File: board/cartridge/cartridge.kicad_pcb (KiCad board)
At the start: 4 copper layers, 66 x 52.8 mm, 24 parts, among them J1 Foxconn_WQ21823-DES1-7F, U1 AMS1117-3.3, U2 STM32G0B0RETx, U3 74LVC1G07, U4 NAU8814Y

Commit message: Place and route MCU power and crystal.
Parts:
- added Y1: X322516MLB4SI, Crystal:Crystal_SMD_3225-4Pin_3.2x2.5mm, F.Cu at (130.0, 102.4)
- C3, C4: value 20p -> 18p
- P1: value ~ -> CardEdge
- moved C6 35.6 mm to (126.2, 100.6)
- moved C5 33.7 mm to (126.2, 102.1)
- moved C3 27.5 mm to (130.1, 104.9)
- moved C4 26.4 mm to (133.0, 102.3), turned to -90 degrees
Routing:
- net /D3: track 31.7 -> 0.00 mm, vias 2 -> 0
- net /D2: track 29.7 -> 0.00 mm, vias 1 -> 0
- net /D1: track 29.1 -> 0.00 mm, vias 2 -> 0
- net /D0: track 28.2 -> 0.00 mm, vias 1 -> 0
- net /D4: track 28.2 -> 0.00 mm, vias 1 -> 0
- net /D6: track 27.1 -> 0.00 mm, vias 1 -> 0
- net /D5: track 29.5 -> 7.11 mm, vias 2 -> 1
- net /D7: track 28.4 -> 9.20 mm, vias 2 -> 1
- net GND: track 30.2 -> 43.3 mm, vias 6 -> 8
- net +3V3: track 8.95 -> 18.4 mm, vias 0 -> 1
- net /OSC_OUT: track 0.00 -> 8.21 mm
- net /OSC_IN: track 0.00 -> 8.11 mm
- net /SWD_~{RST}: track 0.00 -> 4.93 mm

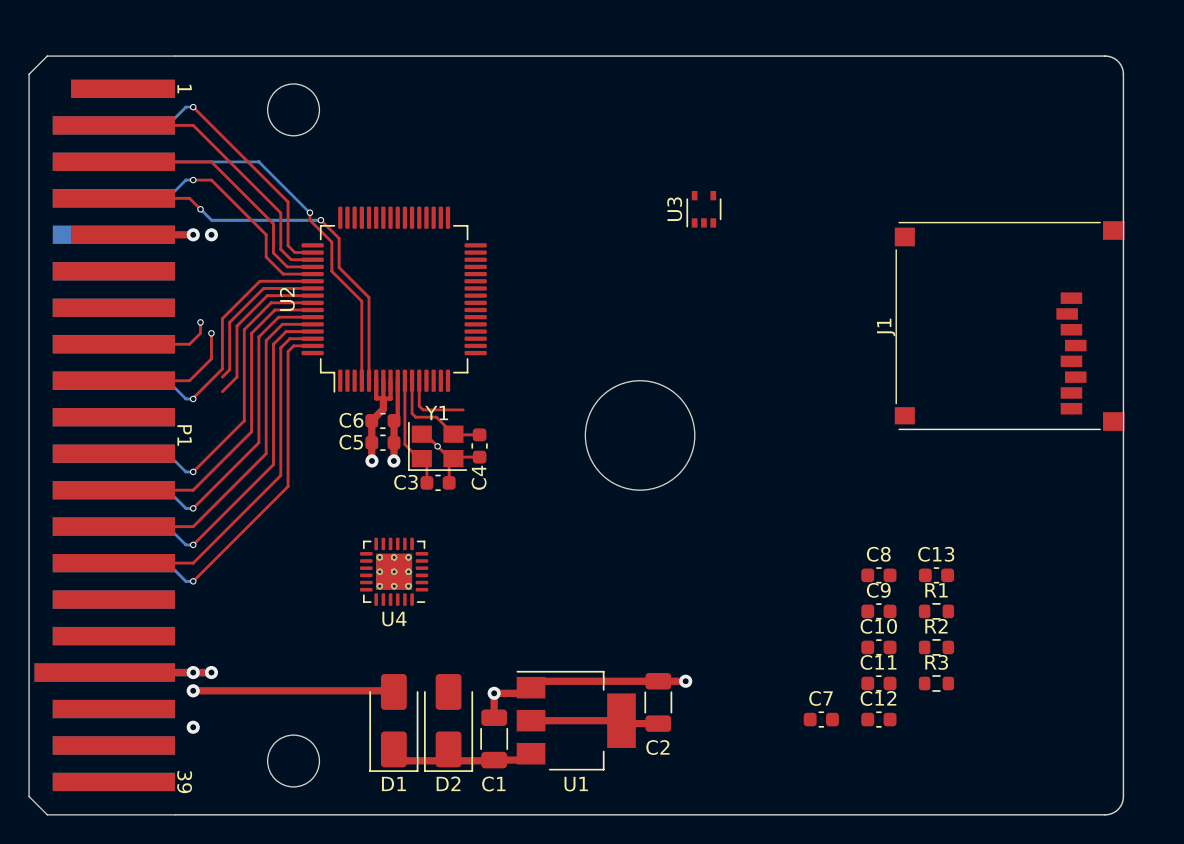
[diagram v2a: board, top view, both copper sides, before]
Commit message: Choose parts for everything plus more routing.
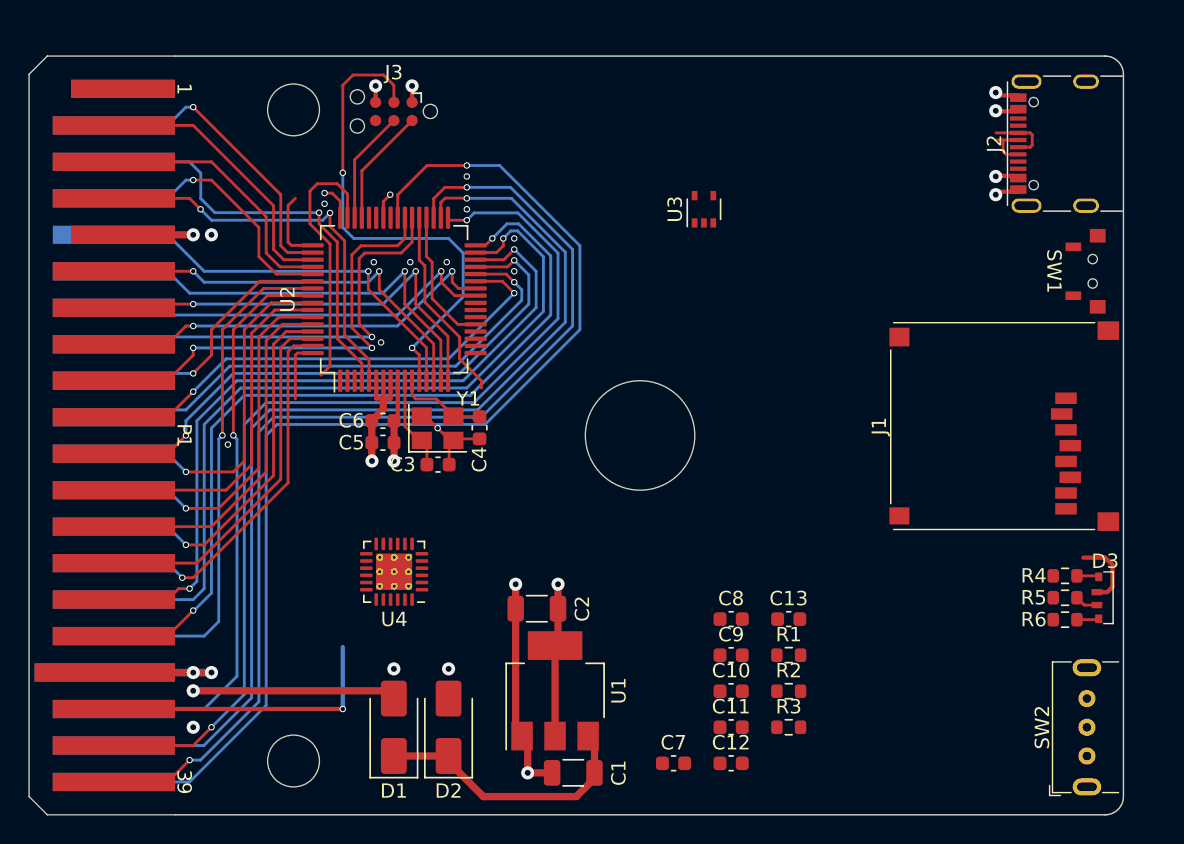
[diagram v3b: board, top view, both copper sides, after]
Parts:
- added D3: FM-3510RGBA-SG, 0Project:FM-3510RGBA-SG, F.Cu at (176.5, 112.9)
- added J2: KH-TYPE-C-16P, 0Project:KH-TYPE-C-16P, F.Cu at (174.1, 81.3)
- added J3: TC2030-NL, Connector:Tag-Connect_TC2030-IDC-NL_2x03_P1.27mm_Vertical, F.Cu at (127.0, 79.0)
- added R4: 100R, Resistor_SMD:R_0603_1608Metric, F.Cu at (173.7, 111.4)
- added R5: 100R, Resistor_SMD:R_0603_1608Metric, F.Cu at (173.7, 112.9)
- added R6: 100R, Resistor_SMD:R_0603_1608Metric, F.Cu at (173.7, 114.4)
- added SW1: TSA002A3518B, 0Project:TSA002A3518B, F.Cu at (175.3, 90.2)
- added SW2: SK12D07VG4, 0Project:SK12D07VG4, F.Cu at (175.3, 121.9)
- D1, D2: value SS12-AT -> SS14
- moved C7 10.7 mm to (146.5, 124.4)
- moved C10 10.7 mm to (150.5, 119.4)
- moved C11 10.7 mm to (150.5, 121.9)
- moved C12 10.7 mm to (150.5, 124.4)
- moved C13 10.7 mm to (154.5, 114.4)
- moved C8 10.7 mm to (150.5, 114.4)
- moved C9 10.7 mm to (150.5, 116.9)
- moved R1 10.7 mm to (154.5, 116.9)
- moved R2 10.7 mm to (154.5, 119.4)
- moved R3 10.7 mm to (154.5, 121.9)
- moved C2 10.7 mm to (137.0, 113.7), turned to 180 degrees
- moved J1 6.98 mm to (161.8, 108.0)
- moved C1 6.00 mm to (139.5, 125.1), turned to 180 degrees
- moved U1 2.55 mm to (138.2, 119.4), turned to 90 degrees
- moved C4 1.27 mm to (133.0, 101.1)
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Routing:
- net /~{SLEN}: track 0.00 -> 79.8 mm, vias 0 -> 1
- net /A15: track 0.00 -> 74.6 mm, vias 0 -> 2
- net /A14: track 0.00 -> 70.9 mm, vias 0 -> 1
- net /A13: track 0.00 -> 68.0 mm, vias 0 -> 2
- net /A12: track 0.00 -> 57.3 mm, vias 0 -> 2
- net /A11: track 0.00 -> 55.1 mm, vias 0 -> 1
- net /A10: track 0.00 -> 52.0 mm, vias 0 -> 2
- net /A2: track 0.00 -> 40.1 mm, vias 0 -> 2
- net /A1: track 0.00 -> 36.2 mm, vias 0 -> 1
- net /A0: track 0.00 -> 34.5 mm, vias 0 -> 2
- net /D6: track 0.00 -> 30.9 mm, vias 0 -> 1
- net /D3: track 0.00 -> 30.6 mm, vias 0 -> 2
- net /D2: track 0.00 -> 30.2 mm, vias 0 -> 1
- net /SWD_~{RST}: track 4.93 -> 34.9 mm, vias 0 -> 2
- net /~{SCS}: track 11.1 -> 40.3 mm, vias 0 -> 1
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
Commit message: Update footprint positions to match JLCPCB.
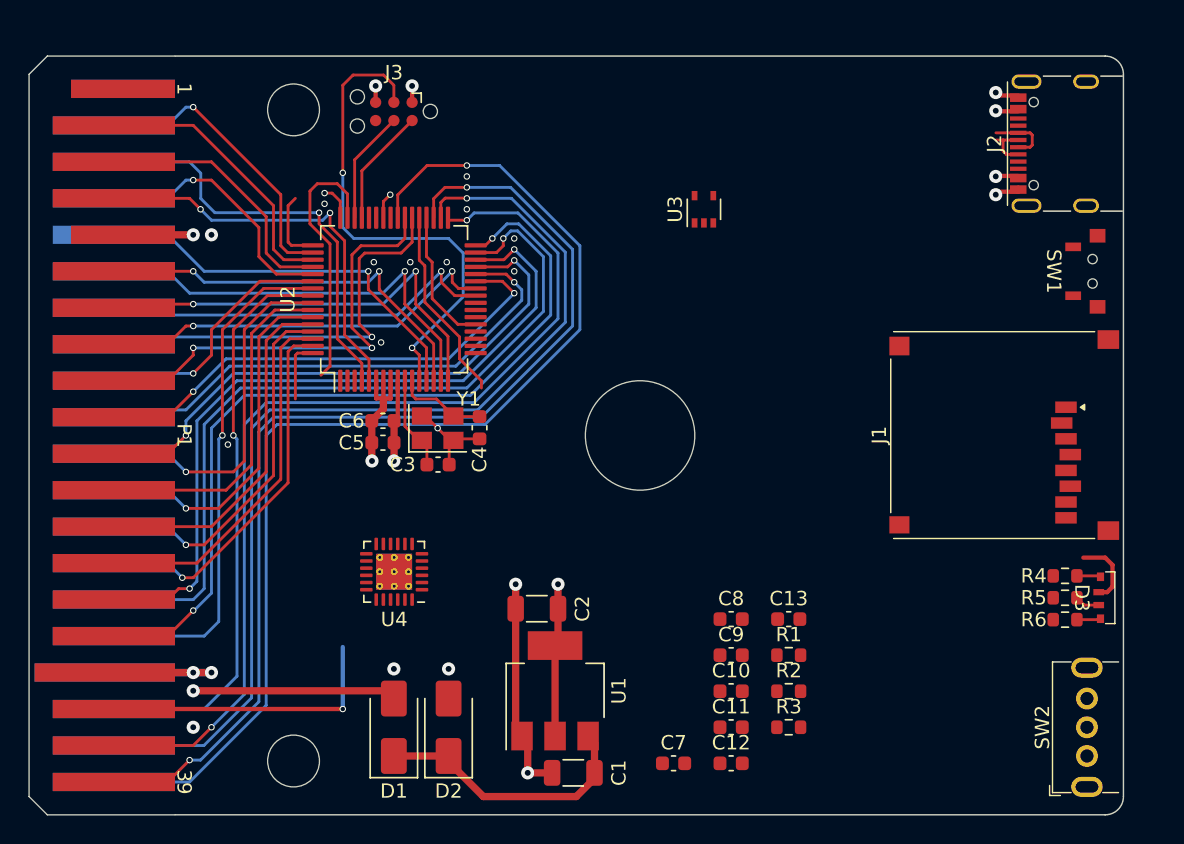
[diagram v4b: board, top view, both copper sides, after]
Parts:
- moved J1 10.0 mm to (169.6, 101.6)
- moved J2 1.31 mm to (172.8, 81.3)
- moved D3 0.39 mm to (176.1, 112.9)
- moved SW1 0.11 mm to (175.2, 90.2)

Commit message: Rip up and try routing as 2 layer.
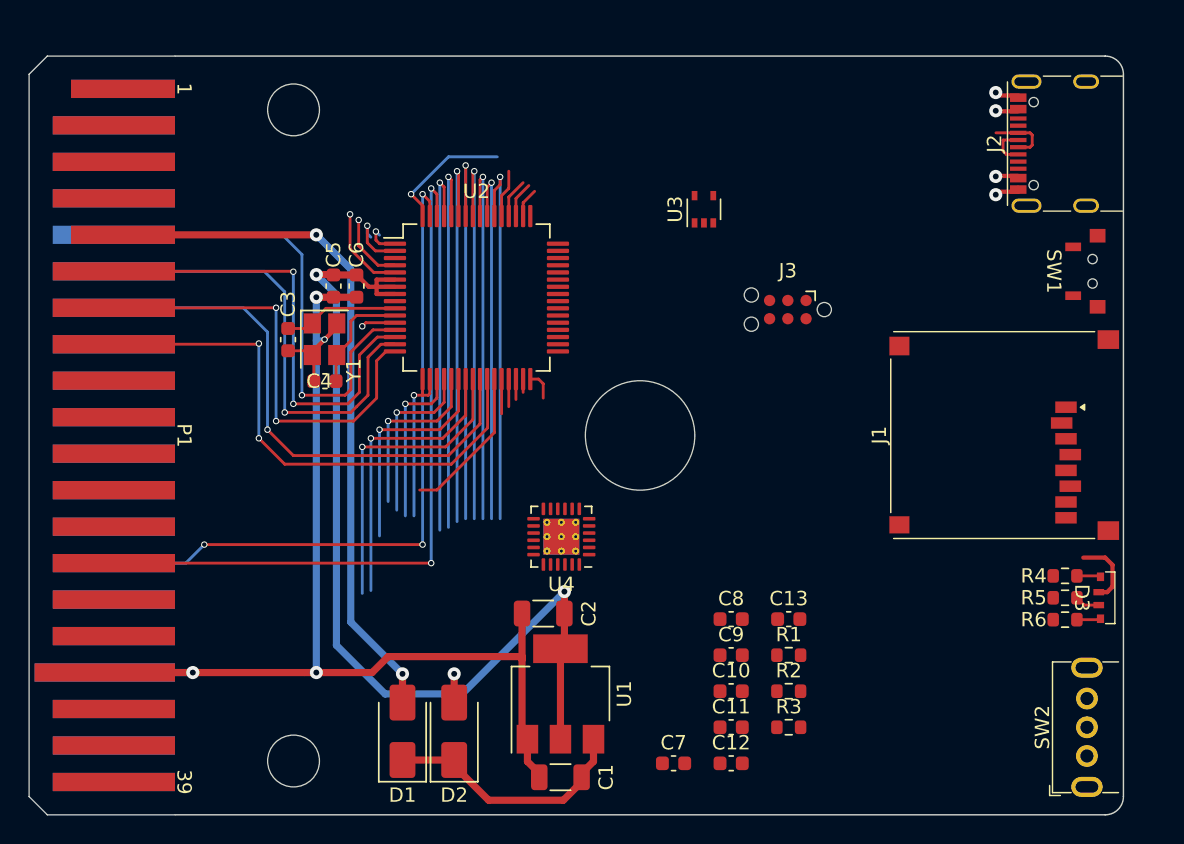
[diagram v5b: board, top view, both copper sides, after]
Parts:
- moved J3 30.7 mm to (154.4, 92.8)
- moved C3 13.6 mm to (119.6, 94.9), turned to -90 degrees
- moved U4 11.9 mm to (138.7, 108.7)
- moved C5 11.4 mm to (122.8, 91.2), turned to -90 degrees
- moved C4 11.2 mm to (122.2, 97.8), turned to 180 degrees
- moved Y1 10.0 mm to (122.2, 94.9), turned to -90 degrees
- moved C6 9.56 mm to (124.4, 91.2), turned to -90 degrees
- moved U2 5.73 mm to (132.8, 92.0), turned to 0 degrees
- moved C1 0.95 mm to (138.6, 125.4)
- moved D1 0.66 mm to (127.6, 122.2)
- moved C2 0.56 mm to (137.4, 114.0)
- moved D2 0.48 mm to (131.2, 122.2)
- moved U1 0.43 mm to (138.6, 119.6)
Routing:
- net /~{SLEN}: track 79.8 -> 0.00 mm, vias 1 -> 0
- net /A15: track 74.6 -> 0.00 mm, vias 2 -> 0
- net /A14: track 70.9 -> 0.00 mm, vias 1 -> 0
- net /A13: track 68.0 -> 0.00 mm, vias 2 -> 0
- net /A12: track 57.3 -> 2.03 mm, vias 2 -> 0
- net /A11: track 55.1 -> 0.92 mm, vias 1 -> 0
- net /A10: track 52.0 -> 1.42 mm, vias 2 -> 0
- net +3V3: track 26.3 -> 71.4 mm, vias 3 -> 2
- net GND: track 47.9 -> 87.5 mm, vias 23 -> 6
- net /A2: track 40.1 -> 1.92 mm, vias 2 -> 0
- net /A1: track 36.2 -> 2.42 mm, vias 1 -> 0
- net /SWD_~{RST}: track 34.9 -> 2.38 mm, vias 2 -> 1
- net /D7: track 31.9 -> 0.00 mm, vias 2 -> 0
- net /D6: track 30.9 -> 0.00 mm, vias 1 -> 0
- net /E: track 29.7 -> 4.88 mm
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- removed copper zone on In1.Cu, net GND
- removed copper zone on In2.Cu, net GND
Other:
- copper layers 4 -> 2

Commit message: Adjust layout based on an actual Tandy cartridge.
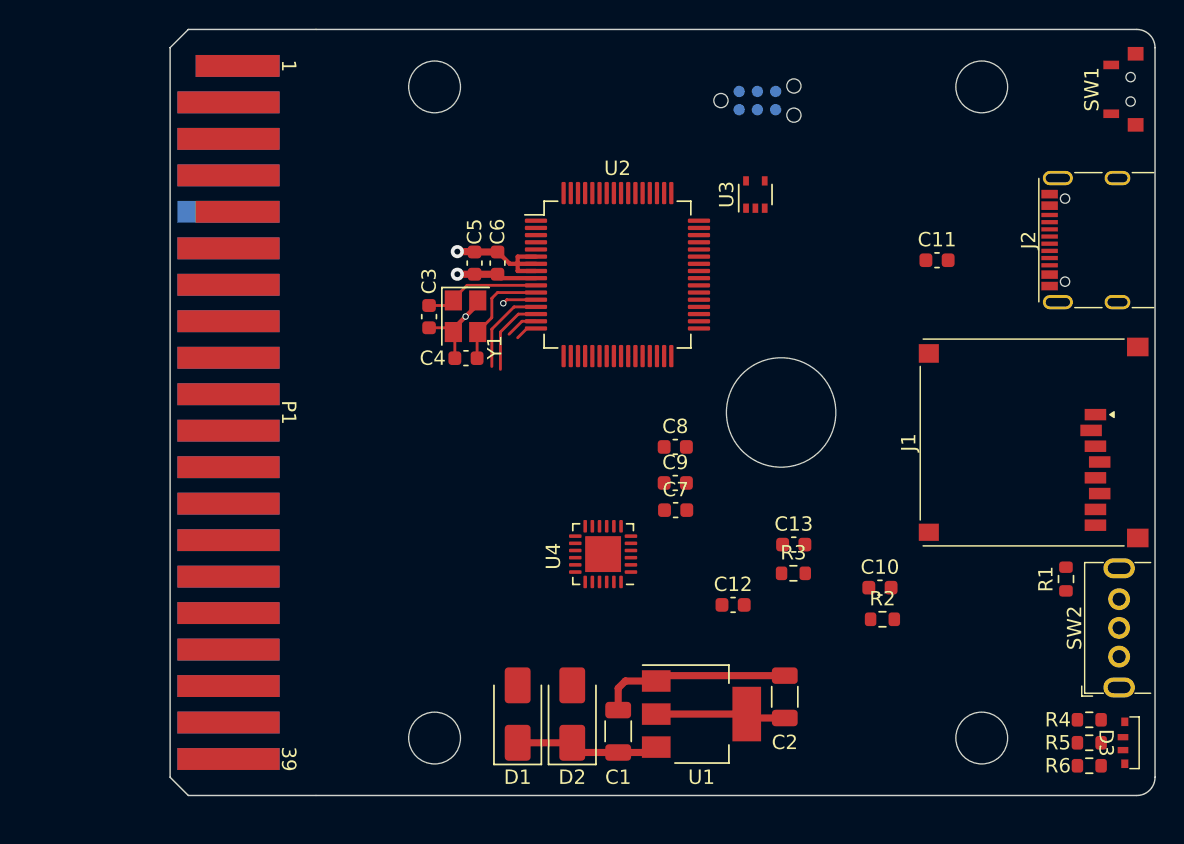
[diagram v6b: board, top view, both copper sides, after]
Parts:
- added MH1: CoCo_MountingHole, 0Local:CoCo_MountingHole, F.Cu at (129.8, 77.3)
- added MH1: CoCo_MountingHole, 0Local:CoCo_MountingHole, F.Cu at (167.9, 77.3)
- added MH1: CoCo_MountingHole, 0Local:CoCo_MountingHole, F.Cu at (167.9, 122.7)
- added MH2: CoCo_MountingHole, 0Local:CoCo_MountingHole, F.Cu at (129.8, 122.7)
- added MH5: CoCo_ClearanceHole, 0Local:CoCo_ClearanceHole, F.Cu at (154.0, 100.0)
- J1: value Foxconn_WQ21823-DES1-7F -> WQ21823-DES1-7F
- J3: moved to B.Cu
- U4: footprint Package_DFN_QFN:VQFN-24-1EP_4x4mm_P0.5mm_EP2.5x2.5mm_ThermalVias -> Package_DFN_QFN:VQFN-24-1EP_4x4mm_P0.5mm_EP2.5x2.5mm
- moved C11 35.5 mm to (164.8, 89.4)
- moved R1 20.0 mm to (173.8, 111.6), turned to 90 degrees
- moved C2 17.8 mm to (154.2, 119.8), turned to 90 degrees
- moved C7 17.6 mm to (146.6, 106.8)
- moved J3 14.7 mm to (152.3, 78.3), turned to 0 degrees
- moved SW1 12.9 mm to (177.8, 77.5)
- moved C10 12.6 mm to (160.8, 112.2)
- moved C9 12.6 mm to (146.6, 104.9)
- moved C8 12.6 mm to (146.6, 102.4)
- moved C12 11.0 mm to (150.6, 113.4)
- moved R3 10.7 mm to (154.8, 111.2)
- moved R6 10.3 mm to (175.4, 124.6)
- moved D3 10.2 mm to (177.8, 123.0)
- moved R5 10.2 mm to (175.4, 123.0)
- moved R4 10.2 mm to (175.4, 121.4)
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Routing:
- net GND: track 87.5 -> 25.7 mm, vias 6 -> 2
- net +3V3: track 71.4 -> 18.4 mm, vias 2 -> 1
- net /A8: track 50.3 -> 0.00 mm, vias 2 -> 0
- net +5V: track 48.5 -> 0.00 mm, vias 2 -> 0
- net /A9: track 48.2 -> 0.00 mm, vias 3 -> 0
- net /D5: track 37.8 -> 0.04 mm, vias 2 -> 0
- net /D4: track 37.8 -> 0.00 mm, vias 1 -> 0
- net /D2: track 32.1 -> 2.25 mm, vias 1 -> 0
- net /D3: track 31.0 -> 1.54 mm, vias 2 -> 0
- net /A4: track 28.1 -> 0.00 mm, vias 1 -> 0
- net /A5: track 27.6 -> 0.00 mm, vias 1 -> 0
- net /A3: track 27.4 -> 0.00 mm, vias 1 -> 0
- net /A6: track 27.2 -> 0.00 mm, vias 1 -> 0
- net /D0: track 33.3 -> 6.32 mm, vias 1 -> 0
- net /R/~{W}: track 26.7 -> 0.00 mm, vias 1 -> 0
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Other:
- board size 66 x 52.8 mm -> 58.4 x 53.3 mm

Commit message: Another attempt at routing.
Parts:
- J3: moved to F.Cu
- moved C10 29.3 mm to (133.0, 103.0), turned to -90 degrees
- moved R2 28.8 mm to (134.6, 103.0), turned to -90 degrees
- moved C13 17.7 mm to (137.2, 107.9)
- moved R3 14.8 mm to (140.4, 107.9), turned to 180 degrees
- moved C11 12.6 mm to (176.6, 93.8)
- moved C12 12.5 mm to (140.4, 106.3)
- moved C9 9.49 mm to (137.2, 106.3), turned to 180 degrees
- moved U4 8.40 mm to (139.1, 101.8)
- moved J3 7.22 mm to (154.4, 85.2), turned to 180 degrees
- moved U3 5.53 mm to (149.8, 79.8), turned to -90 degrees
- moved C7 4.64 mm to (144.1, 102.9)
- moved C8 3.67 mm to (143.4, 100.6), turned to 90 degrees
- moved C3 0.40 mm to (129.5, 92.9)
- moved C4 0.40 mm to (132.0, 95.8)
- moved U2 0.40 mm to (142.6, 90.0)
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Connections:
- net /USB_DM renamed /USB_DN
- U4 pad 20: unconnected-(U4-VDDSPK-Pad20) -> +3V3
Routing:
- net GND: track 25.7 -> 176.5 mm, vias 2 -> 8
- net VBUS: track 0.00 -> 76.6 mm, vias 0 -> 3
- net +5V: track 0.00 -> 69.7 mm, vias 0 -> 2
- net +3V3: track 18.4 -> 67.6 mm, vias 1 -> 3
- net /~{NMI}: track 0.00 -> 37.4 mm, vias 0 -> 1
- net /~{HALT}: track 0.00 -> 36.4 mm
- net /~{RESET}: track 0.00 -> 35.1 mm, vias 0 -> 1
- net /~{CART}: track 0.00 -> 33.3 mm, vias 0 -> 1
- net /USB_DN: track 0.00 -> 27.1 mm
- net /E: track 0.00 -> 26.3 mm, vias 0 -> 1
- net /USB_DP: track 0.00 -> 26.3 mm
- net /Q: track 0.00 -> 24.6 mm
- net /I2S_MCLK: track 0.00 -> 16.3 mm
- net /I2S_FS: track 0.00 -> 16.0 mm, vias 0 -> 2
- net /I2C_SDA: track 0.00 -> 11.7 mm, vias 0 -> 2
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
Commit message: Move CoCo footprints up to project.
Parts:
- MH1 (x3), MH2: footprint 0Local:CoCo_MountingHole -> 0Project:CoCo_MountingHole
- MH5: footprint 0Local:CoCo_ClearanceHole -> 0Project:CoCo_ClearanceHole
- P1: value CardEdge -> Card Edge; footprint 0Local:CoCo_Cart -> 0Project:CoCo_Cart
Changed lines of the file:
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@@
     )
   )
-  (footprint "0Local:CoCo_MountingHole" locked (layer "F.Cu")
+  (footprint "0Project:CoCo_MountingHole" locked (layer "F.Cu")
     (at 129.835 77.3305)
     (attr through_hole board_only exclude_from_pos_files exclude_from_bom)
@@
     )
   )
-  (footprint "0Local:CoCo_MountingHole" locked (layer "F.Cu")
+  (footprint "0Project:CoCo_MountingHole" locked (layer "F.Cu")
     (at 167.93374 77.3305)
     (attr through_hole board_only exclude_from_pos_files exclude_from_bom)
@@
     )
   )
-  (footprint "0Local:CoCo_Cart" locked (layer "F.Cu")
+  (footprint "0Project:CoCo_Cart" locked (layer "F.Cu")
     (at 111.42 100 -90)
     (descr "TRS-80 Color Computer 1-3 Cartridge Connector")
@@
         (effects (font (size 1 1) (thickness 0.15)))
     )
-    (fp_text value "CardEdge" (at 0 -0.635 -90 unlocked) (layer "F.Fab") hide
-        (effects (font (size 1 1) (thickness 0.15)))
+    (fp_text value "Card Edge" (at 0 -0.635 -90 unlocked) (layer "F.Fab") hide
+        (effects (font (size 1 1) (thickness 0.15)))
+    )
+    (fp_text user "2" (at -24.13 -8.255 -90 unlocked) (layer "B.SilkS")
+        (effects (font (size 1 1) (thickness 0.15)) (justify mirror))
     )
     (fp_text user "40" (at 24.13 -8.255 -90 unlocked) (layer "B.SilkS")
-        (effects (font (size 1 1) (thickness 0.15)) (justify mirror))
-    )
-    (fp_text user "2" (at -24.13 -8.255 -90 unlocked) (layer "B.SilkS")
         (effects (font (size 1 1) (thickness 0.15)) (justify mirror))
     )
@@
       (net 44 "/~{SLEN}") (pinfunction "~{SLENB}") (pintype "input"))
   )
-  (footprint "0Local:CoCo_MountingHole" locked (layer "F.Cu")
+  (footprint "0Project:CoCo_MountingHole" locked (layer "F.Cu")
     (at 129.835 122.6695)
     (attr through_hole board_only exclude_from_pos_files exclude_from_bom)
@@
     (pad "" np_thru_hole circle locked (at 0 0) (size 5.715 5.715) (drill 3.6068) (layers "*.Mask"))
   )
-  (footprint "0Local:CoCo_ClearanceHole" locked (layer "F.Cu")
+  (footprint "0Project:CoCo_ClearanceHole" locked (layer "F.Cu")
     (at 153.965 100)
     (attr through_hole board_only exclude_from_pos_files exclude_from_bom)
@@
     )
   )
-  (footprint "0Local:CoCo_MountingHole" locked (layer "F.Cu")
+  (footprint "0Project:CoCo_MountingHole" locked (layer "F.Cu")
     (at 167.93374 122.6695)
     (attr through_hole board_only exclude_from_pos_files exclude_from_bom)
